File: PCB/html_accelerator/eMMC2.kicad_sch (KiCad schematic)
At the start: 15 parts, among them U5 EMMC_4G, U6 EMMC_4G, U8 AU6438BS, Y3 12MHz

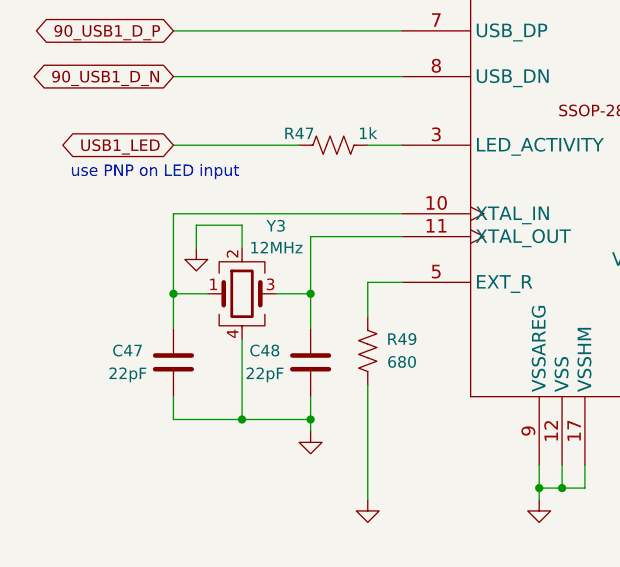
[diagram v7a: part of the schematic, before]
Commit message: Additional routing greebles, cleanup and gerber export with BOM
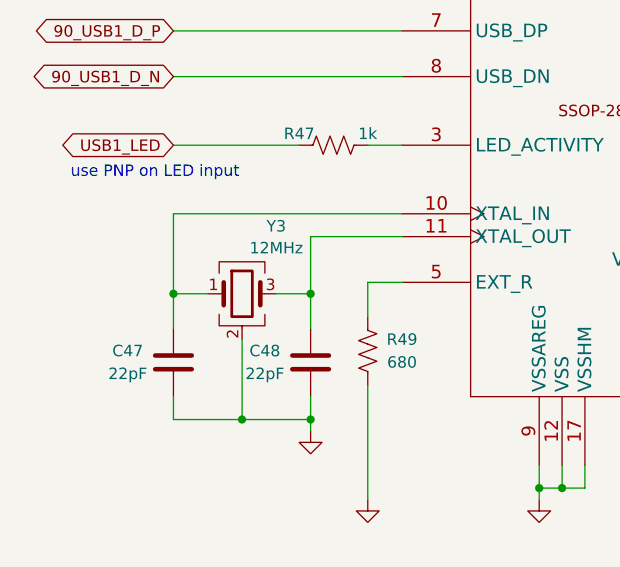
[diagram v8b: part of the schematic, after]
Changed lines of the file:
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@@
-	(wire
-		(pts
-			(xy 36.83 87.63) (xy 36.83 90.17)
-		)
-		(stroke
-			(width 0)
-			(type default)
-		)
-	)
 	(wire
 		(pts
@@
 	(wire
 		(pts
-			(xy 41.91 87.63) (xy 36.83 87.63)
-		)
-		(stroke
-			(width 0)
-			(type default)
-		)
-	)
-	(wire
-		(pts
 			(xy 196.85 109.22) (xy 199.39 109.22)
 		)
@@
 		(pts
 			(xy 34.29 95.25) (xy 38.1 95.25)
-		)
-		(stroke
-			(width 0)
-			(type default)
-		)
-	)
-	(wire
-		(pts
-			(xy 41.91 90.17) (xy 41.91 87.63)
 		)
 		(stroke
@@
 				)
 				(justify right)
-			)
-		)
-	)
-	(symbol
-		(lib_id "power:GND")
-		(at 36.83 90.17 0)
-		(unit 1)
-		(body_style 1)
-		(exclude_from_sim no)
-		(in_bom yes)
-		(on_board yes)
-		(in_pos_files yes)
-		(dnp no)
-		(fields_autoplaced yes)
-		(property "Reference" "#PWR053"
-			(at 36.83 96.52 0)
-			(hide yes)
-			(show_name no)
-			(do_not_autoplace no)
-			(effects
-				(font
-					(size 1.27 1.27)
-				)
-			)
-		)
-		(property "Value" "GND"
-			(at 36.83 94.3055 0)
-			(hide yes)
-			(show_name no)
-			(do_not_autoplace no)
-			(effects
-				(font
-					(size 1.27 1.27)
-				)
-			)
-		)
-		(property "Footprint" ""
-			(at 36.83 90.17 0)
-			(hide yes)
-			(show_name no)
-			(do_not_autoplace no)
-			(effects
-				(font
-					(size 1.27 1.27)
-				)
-			)
-		)
-		(property "Datasheet" ""
-			(at 36.83 90.17 0)
-			(hide yes)
-			(show_name no)
-			(do_not_autoplace no)
-			(effects
-				(font
-					(size 1.27 1.27)
-				)
-			)
-		)
-		(property "Description" ""
-			(at 36.83 90.17 0)
-			(show_name no)
-			(do_not_autoplace no)
-			(effects
-				(font
-					(size 1.27 1.27)
-				)
-			)
-		)
-		(pin "1"
-		)
-		(instances
-			(project "html_accelerator"
-				(path "/12b3a7c9-141f-40ba-9ebb-094b58bfa6c7/a3cdbafc-e5e5-4b5b-8c38-75acb12ca284"
-					(reference "#PWR053")
-					(unit 1)
-				)
 			)
 		)
@@
 			)
 		)
-		(property "Description" ""
+		(property "Description" "Four pin crystal, GND on pins 2 and 4"
 			(at 41.91 95.25 0)
-			(show_name no)
-			(do_not_autoplace no)
+			(hide yes)
+			(show_name no)
+			(do_not_autoplace no)
